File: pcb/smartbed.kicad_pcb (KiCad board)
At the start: 2 copper layers, 1 part, among them U1 ATSAMD21J18A

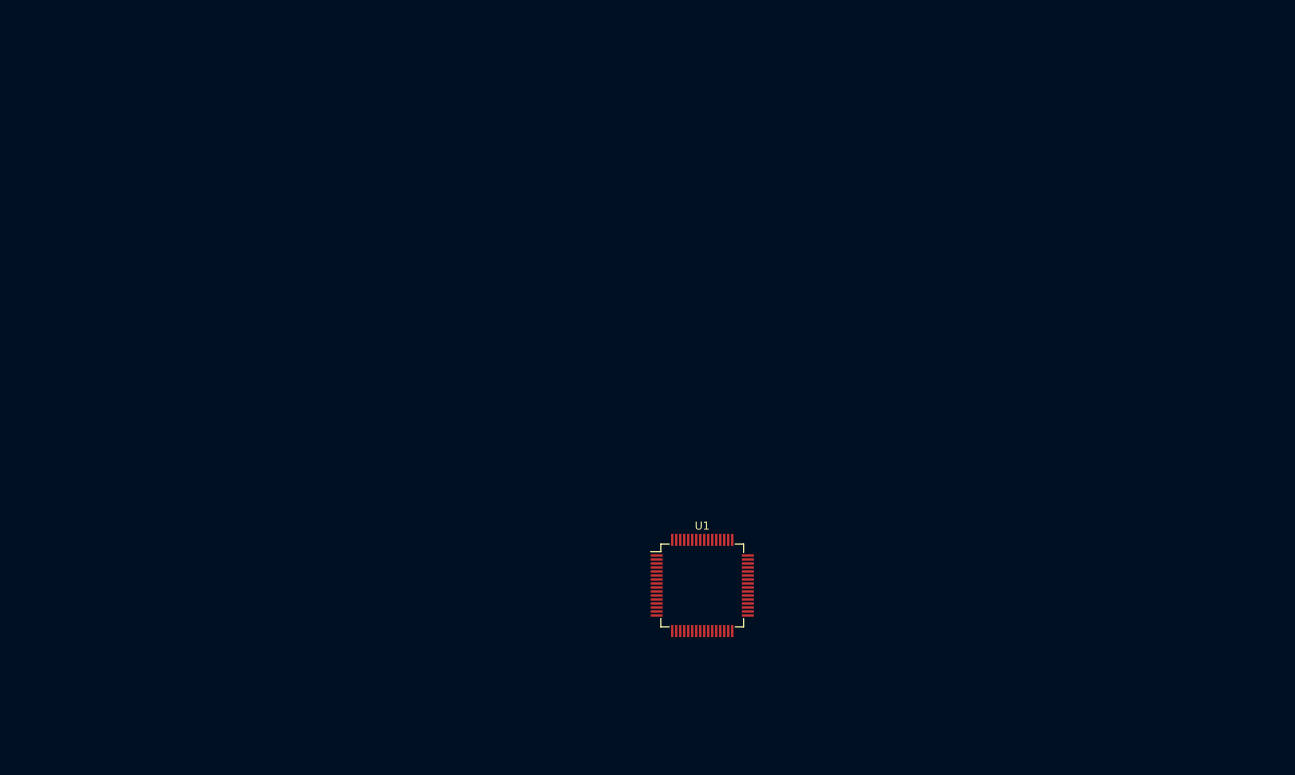
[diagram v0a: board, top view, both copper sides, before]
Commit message: Assigned footprints, started PCB
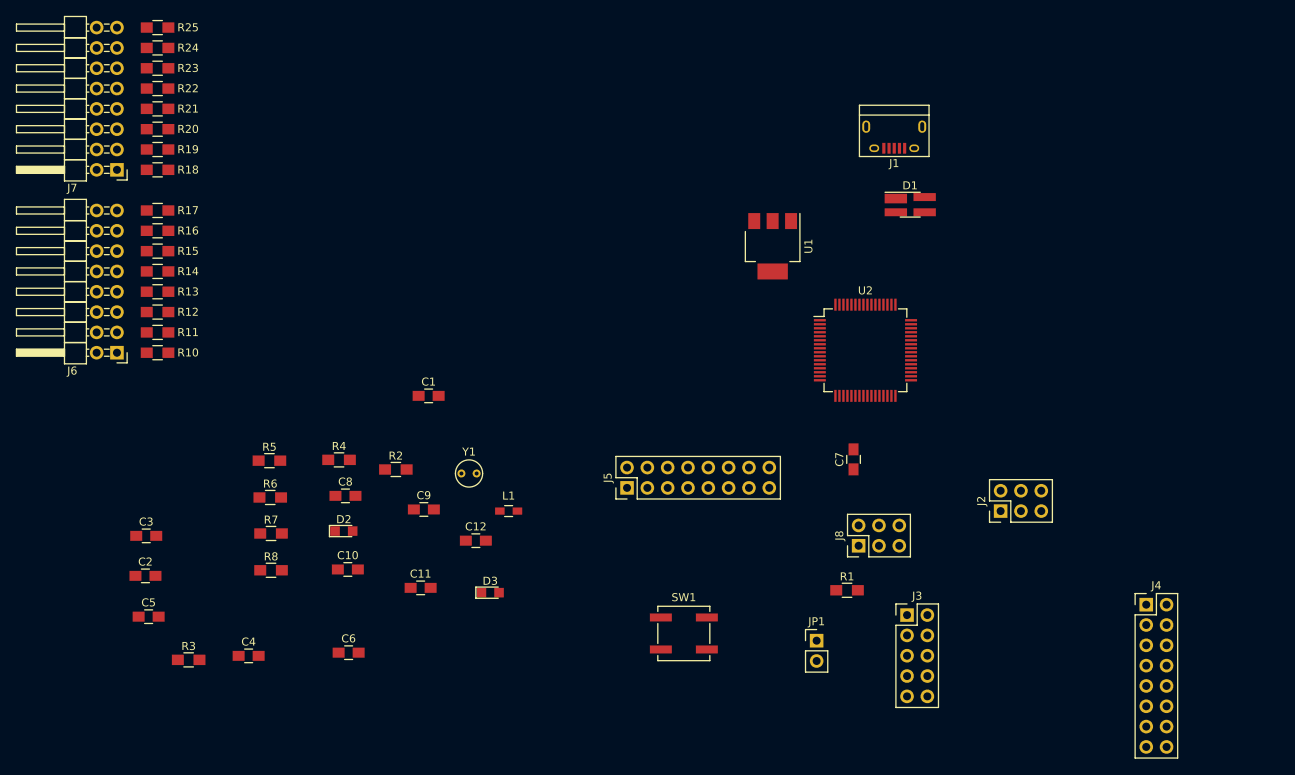
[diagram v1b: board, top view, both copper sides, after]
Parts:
- added C1: 100nF, Capacitors_SMD:C_0805_HandSoldering, F.Cu at (105.0, 83.5)
- added C10: 100nF, Capacitors_SMD:C_0805_HandSoldering, F.Cu at (94.9, 105.2)
- added C11: 100nF, Capacitors_SMD:C_0805_HandSoldering, F.Cu at (104.0, 107.5)
- added C12: 100nF, Capacitors_SMD:C_0805_HandSoldering, F.Cu at (110.9, 101.6)
- added C2: 6.8pF, Capacitors_SMD:C_0805_HandSoldering, F.Cu at (69.6, 106.0)
- added C3: 100nF, Capacitors_SMD:C_0805_HandSoldering, F.Cu at (69.7, 101.0)
- added C4: 100nF, Capacitors_SMD:C_0805_HandSoldering, F.Cu at (82.5, 116.0)
- added C5: 100nF, Capacitors_SMD:C_0805_HandSoldering, F.Cu at (70.0, 111.1)
- added C6: 6.8pF, Capacitors_SMD:C_0805_HandSoldering, F.Cu at (95.0, 115.6)
- added C7: 100nF, Capacitors_SMD:C_0805_HandSoldering, F.Cu at (158.1, 91.4)
- added C8: 10uF, Capacitors_SMD:C_0805_HandSoldering, F.Cu at (94.6, 96.0)
- added C9: 100nF, Capacitors_SMD:C_0805_HandSoldering, F.Cu at (104.4, 97.7)
- added D1: PRTR5V0U2X, TO_SOT_Packages_SMD:SOT-143_Handsoldering, F.Cu at (165.2, 59.6)
- added D2: LED G, LEDs:LED_0805, F.Cu at (94.4, 100.4)
- added D3: LED G, LEDs:LED_0805, F.Cu at (112.7, 108.1)
- added J1: USB_MICRO_A, Connectors:USB_Micro-B, F.Cu at (163.2, 51.2)
- added J2: SBBUS_1, Pin_Headers:Pin_Header_Straight_2x03_Pitch2.54mm, F.Cu at (176.5, 97.9)
- added J3: DBGCON, Pin_Headers:Pin_Header_Straight_2x05_Pitch2.54mm, F.Cu at (164.8, 110.9)
- added J4: GPIOCON, Pin_Headers:Pin_Header_Straight_2x08_Pitch2.54mm, F.Cu at (194.7, 109.6)
- added J5: GPIOCON, Pin_Headers:Pin_Header_Straight_2x08_Pitch2.54mm, F.Cu at (129.8, 95.0)
- added J6: FSRCON1, Pin_Headers:Pin_Header_Angled_2x08_Pitch2.54mm, F.Cu at (66.0, 78.1)
- added J7: FSRCON2, Pin_Headers:Pin_Header_Angled_2x08_Pitch2.54mm, F.Cu at (66.0, 55.2)
- added J8: SBBUS_2, Pin_Headers:Pin_Header_Straight_2x03_Pitch2.54mm, F.Cu at (158.8, 102.2)
- added JP1: JMP, Pin_Headers:Pin_Header_Straight_1x02_Pitch2.54mm, F.Cu at (153.5, 114.1)
- added L1: FeBead, Inductors_SMD:L_0603_HandSoldering, F.Cu at (115.0, 97.9)
- added R1: 4.7K, Resistors_SMD:R_0805_HandSoldering, F.Cu at (157.3, 107.8)
- added R10: 10K, Resistors_SMD:R_0805_HandSoldering, F.Cu at (71.1, 78.1)
- added R11: 10K, Resistors_SMD:R_0805_HandSoldering, F.Cu at (71.1, 75.6)
- added R12: 10K, Resistors_SMD:R_0805_HandSoldering, F.Cu at (71.1, 73.0)
- added R13: 10K, Resistors_SMD:R_0805_HandSoldering, F.Cu at (71.1, 70.5)
- added R14: 10K, Resistors_SMD:R_0805_HandSoldering, F.Cu at (71.1, 67.9)
- added R15: 10K, Resistors_SMD:R_0805_HandSoldering, F.Cu at (71.1, 65.4)
- added R16: 10K, Resistors_SMD:R_0805_HandSoldering, F.Cu at (71.1, 62.9)
- added R17: 10K, Resistors_SMD:R_0805_HandSoldering, F.Cu at (71.1, 60.3)
- added R18: 10K, Resistors_SMD:R_0805_HandSoldering, F.Cu at (71.1, 55.2)
- added R19: 10K, Resistors_SMD:R_0805_HandSoldering, F.Cu at (71.1, 52.7)
- added R2: 100k, Resistors_SMD:R_0805_HandSoldering, F.Cu at (100.9, 92.7)
- added R20: 10K, Resistors_SMD:R_0805_HandSoldering, F.Cu at (71.1, 50.2)
- added R21: 10K, Resistors_SMD:R_0805_HandSoldering, F.Cu at (71.1, 47.6)
- added R22: 10K, Resistors_SMD:R_0805_HandSoldering, F.Cu at (71.1, 45.1)
- added R23: 10K, Resistors_SMD:R_0805_HandSoldering, F.Cu at (71.1, 42.5)
- added R24: 10K, Resistors_SMD:R_0805_HandSoldering, F.Cu at (71.1, 40.0)
- added R25: 10K, Resistors_SMD:R_0805_HandSoldering, F.Cu at (71.1, 37.5)
- added R3: 4.7K, Resistors_SMD:R_0805_HandSoldering, F.Cu at (75.0, 116.5)
- added R4: 39R, Resistors_SMD:R_0805_HandSoldering, F.Cu at (93.8, 91.5)
- added R5: 30k, Resistors_SMD:R_0805_HandSoldering, F.Cu at (85.1, 91.6)
- added R6: 47k, Resistors_SMD:R_0805_HandSoldering, F.Cu at (85.2, 96.2)
- added R7: 330R, Resistors_SMD:R_0805_HandSoldering, F.Cu at (85.3, 100.7)
- added R8: 330R, Resistors_SMD:R_0805_HandSoldering, F.Cu at (85.3, 105.3)
- added SW1: SW_SPST, Buttons_Switches_SMD:SW_SPST_B3SL-1002P, F.Cu at (136.9, 113.2)
- added U2: ATSAMD21J18A, Housings_QFP:TQFP-64_10x10mm_Pitch0.5mm, F.Cu at (159.6, 77.8)
- added Y1: 32.768kHz, Crystals:Crystal_Round_d3.0mm_Vertical, F.Cu at (109.1, 93.2)
- U1: value ATSAMD21J18A -> LD1117S33CTR; footprint Housings_QFP:TQFP-64_10x10mm_Pitch0.5mm -> TO_SOT_Packages_SMD:SOT-223
- moved U1 43.3 mm to (148.0, 64.8), turned to 270 degrees
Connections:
- U1 pad 1: Net-(U1-Pad1) -> GND
- U1 pad 2: Net-(U1-Pad2) -> +3V3
- U1 pad 3: Net-(U1-Pad3) -> +5V
- U1 pad 4: Net-(U1-Pad4) -> (no net)

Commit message: Biggest part of board done
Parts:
- C1, C10, C11, C12, C2, C3, C4, C5, C6, C7, C8, C9: footprint Capacitors_SMD:C_0805_HandSoldering -> Capacitors_SMD:C_0603_HandSoldering
- moved J7 133.5 mm to (198.7, 69.9), turned to 0 degrees
- moved R24 132.4 mm to (195.9, 84.4), turned to 90 degrees
- moved R25 131.6 mm to (193.6, 85.7), turned to 90 degrees
- moved R22 129.3 mm to (195.9, 79.0), turned to 90 degrees
- moved R23 128.2 mm to (193.6, 80.3), turned to 90 degrees
- moved R20 127.0 mm to (195.9, 73.7), turned to 90 degrees
- moved R21 125.5 mm to (193.6, 75.0), turned to 90 degrees
- moved R18 125.5 mm to (195.9, 68.4), turned to 270 degrees
- moved R19 123.7 mm to (193.6, 69.7), turned to 90 degrees
- moved R8 119.3 mm to (191.8, 51.5), turned to 270 degrees
- moved C4 116.1 mm to (181.5, 55.3), turned to 270 degrees
- moved R7 115.0 mm to (189.2, 51.5), turned to 270 degrees
- moved D2 104.5 mm to (189.2, 56.5), turned to 90 degrees
- moved C3 98.3 mm to (157.5, 56.8), turned to 90 degrees
- moved D3 94.4 mm to (191.8, 56.5), turned to 90 degrees
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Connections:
- D1 pad 2: D+ -> D-
- D1 pad 3: D- -> D+
- J6 pad 1: FSR0 -> FSR7
- J6 pad 11: FSR5 -> FSR2
- J6 pad 13: FSR6 -> FSR1
- J6 pad 15: FSR7 -> FSR0
- J6 pad 3: FSR1 -> FSR6
- J6 pad 5: FSR2 -> FSR5
- J6 pad 7: FSR3 -> FSR4
- J6 pad 9: FSR4 -> FSR3
- R10 pad 1: FSR0 -> FSR7
- R11 pad 1: FSR1 -> FSR6
- R12 pad 1: FSR2 -> FSR5
- R13 pad 1: FSR3 -> FSR4
- R14 pad 1: FSR4 -> FSR3
- R15 pad 1: FSR5 -> FSR2
- R16 pad 1: FSR6 -> FSR1
- R17 pad 1: FSR7 -> FSR0
- U2 pad 10: FSR15 -> FSR1
- U2 pad 3: FSR0 -> FSR12
- U2 pad 4: FSR1 -> FSR13
- U2 pad 5: FSR12 -> FSR14
- U2 pad 6: FSR13 -> FSR15
- U2 pad 9: FSR14 -> FSR0
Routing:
- net GND: track 0.00 -> 374.7 mm, vias 0 -> 4
- net +3V3: track 0.00 -> 233.2 mm, vias 0 -> 7
- net +5V: track 0.00 -> 95.1 mm, vias 0 -> 1
- net FSR15: track 0.00 -> 49.8 mm, vias 0 -> 2
- net FSR14: track 0.00 -> 49.4 mm, vias 0 -> 2
- net FSR13: track 0.00 -> 48.2 mm, vias 0 -> 2
- net RESET: track 0.00 -> 47.8 mm, vias 0 -> 2
- net FSR8: track 0.00 -> 47.7 mm, vias 0 -> 2
- net FSR12: track 0.00 -> 47.5 mm, vias 0 -> 2
- net FSR11: track 0.00 -> 46.9 mm, vias 0 -> 2
- net FSR9: track 0.00 -> 45.9 mm, vias 0 -> 2
- net FSR10: track 0.00 -> 45.0 mm, vias 0 -> 2
- net DBGLED: track 0.00 -> 44.6 mm, vias 0 -> 2
- net FSR6: track 0.00 -> 43.3 mm
- net FSR7: track 0.00 -> 43.3 mm
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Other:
- net class PWR added: clearance 0.2, trace_width 0.4, via_dia 0.6, via_drill 0.4
- net class uProc added: clearance 0.1, trace_width 0.1, via_dia 0.6, via_drill 0.4
- rule trace_min: 0.2 -> 0.1

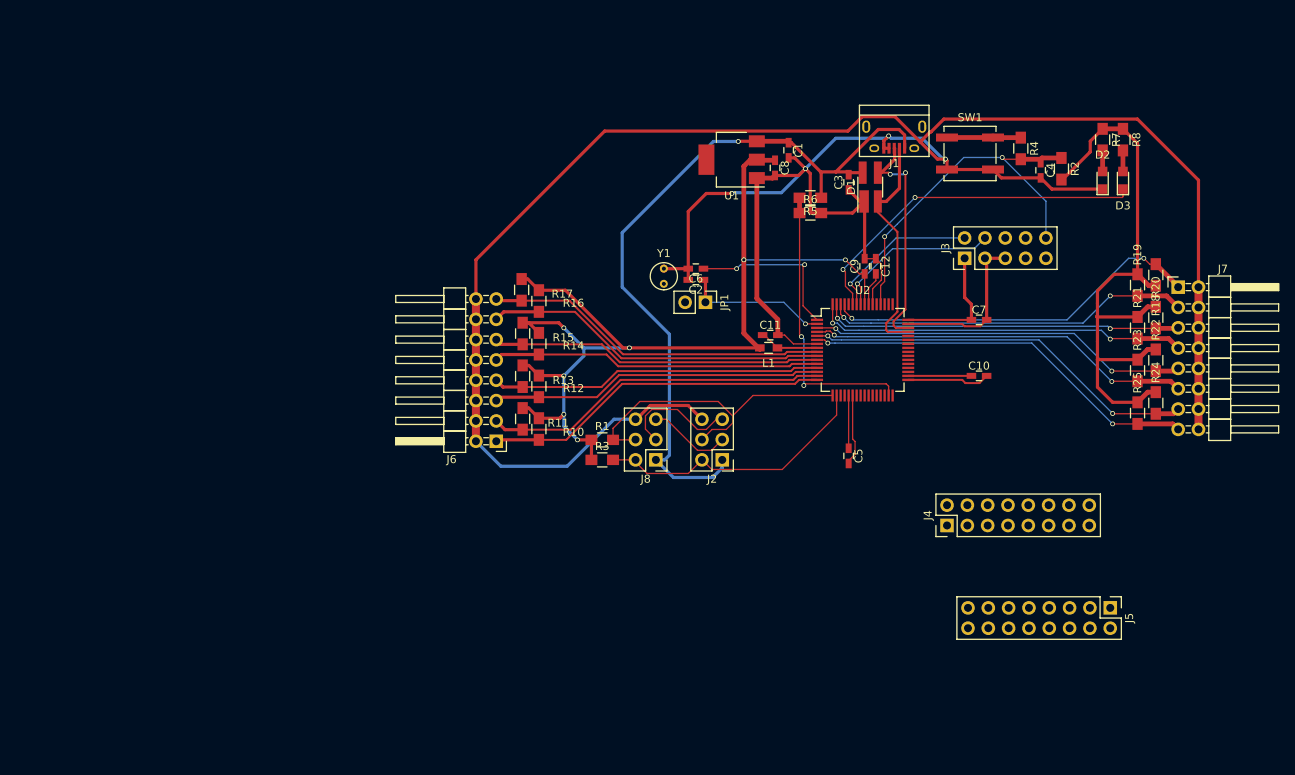
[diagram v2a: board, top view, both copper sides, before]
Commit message: Connected most of the traces
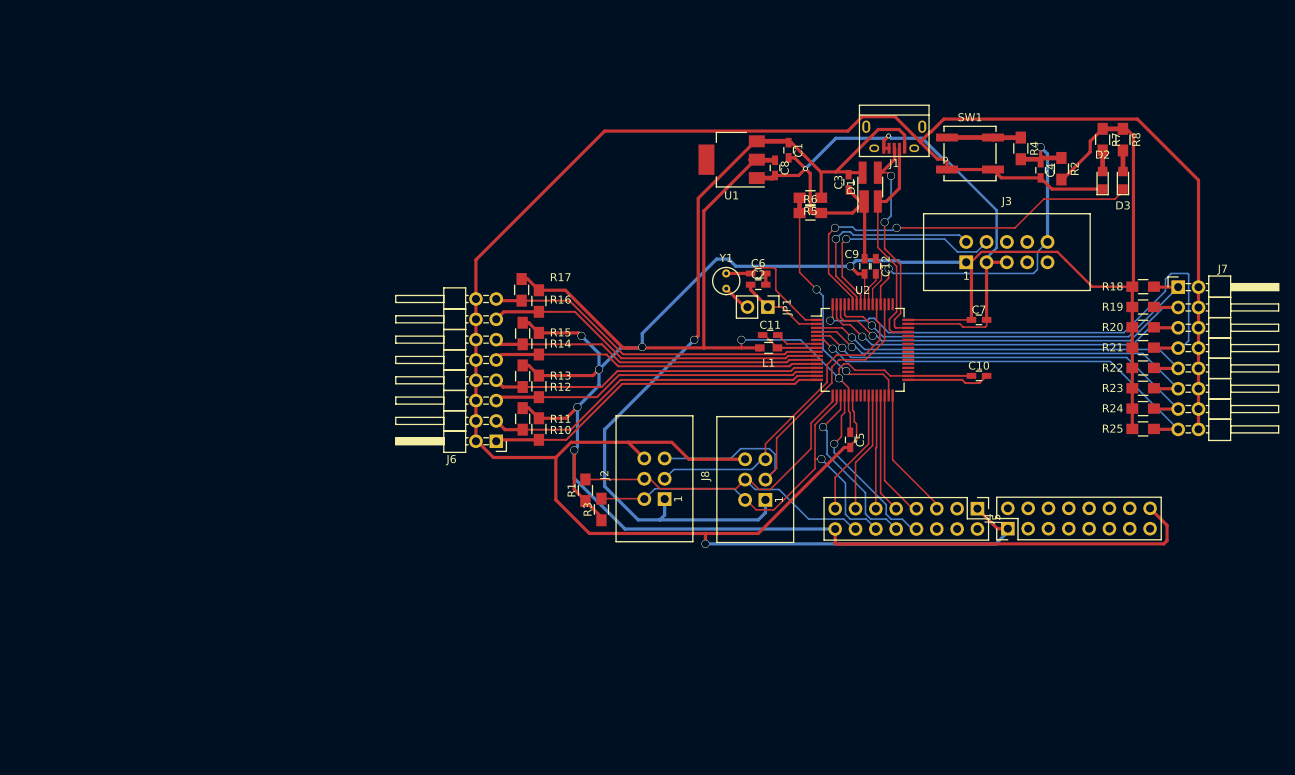
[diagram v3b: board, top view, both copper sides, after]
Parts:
- J2, J8: footprint Pin_Headers:Pin_Header_Straight_2x03_Pitch2.54mm -> Connectors:IDC_Header_Straight_6pins
- J3: footprint Pin_Headers:Pin_Header_Straight_2x05_Pitch2.54mm -> Connectors:IDC_Header_Straight_10pins
- Y1: value 32.768kHz -> Crystal
- moved J5 20.7 mm to (173.6, 97.6)
- moved J8 14.6 mm to (147.1, 96.5), turned to 90 degrees
- moved J2 8.71 mm to (134.5, 96.4), turned to 90 degrees
- moved JP1 7.82 mm to (147.4, 72.4)
- moved C6 7.82 mm to (146.2, 68.2), turned to 0 degrees
- moved C2 7.82 mm to (146.2, 69.6), turned to 0 degrees
- moved Y1 7.82 mm to (142.2, 70.1)
- moved J4 7.61 mm to (177.4, 100.1)
- moved R1 6.64 mm to (124.6, 95.3), turned to 90 degrees
- moved R3 6.20 mm to (126.6, 97.7), turned to 90 degrees
- moved R19 2.83 mm to (194.3, 72.4), turned to 180 degrees
- moved R21 2.58 mm to (194.3, 77.5), turned to 180 degrees
- moved R23 2.34 mm to (194.3, 82.5), turned to 180 degrees
- moved R18 2.16 mm to (194.3, 69.8), turned to 180 degrees
- moved R25 2.10 mm to (194.3, 87.6), turned to 180 degrees
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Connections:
- C2 pad 2: GND -> Net-(C2-Pad2)
- C6 pad 2: GND -> Net-(C2-Pad2)
- Y1 pad 2: GND -> XIN
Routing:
- net +3V3: track 233.2 -> 391.9 mm, vias 7 -> 8
- net GND: track 374.7 -> 438.7 mm
- net SENSE_OUT: track 15.0 -> 48.3 mm
- net SENSE_IN: track 10.5 -> 41.1 mm
- net PA11: track 0.00 -> 22.6 mm, vias 0 -> 1
- net PA10: track 0.00 -> 22.5 mm, vias 0 -> 1
- net SCL: track 35.3 -> 54.3 mm, vias 0 -> 1
- net FSR11: track 46.9 -> 64.9 mm, vias 2 -> 1
- net PA15: track 0.00 -> 16.4 mm
- net PA13: track 0.00 -> 16.1 mm
- net SDA: track 40.5 -> 56.6 mm
- net PB13: track 0.00 -> 15.9 mm
- net PB14: track 0.00 -> 15.0 mm
- net PA12: track 0.00 -> 15.0 mm
- net PB15: track 0.00 -> 14.2 mm
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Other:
- net class Default: trace_width 0.25 -> 0.2; via_dia 0.6 -> 1; via_drill 0.4 -> 0.9
- net class PWR removed
- net class uProc removed
- rule trace_min: 0.1 -> 0.2
- rule via_min_drill: 0.3 -> 0.9
- rule via_min_size: 0.4 -> 0.6

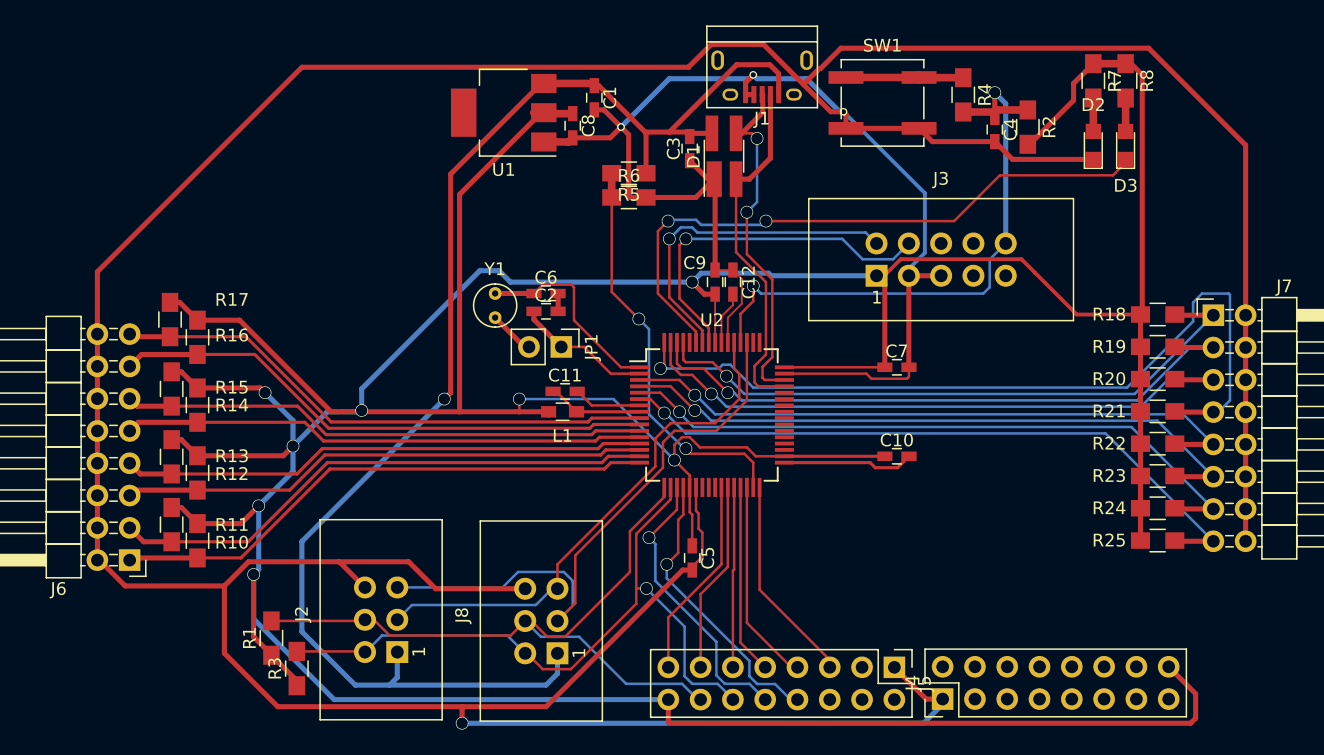
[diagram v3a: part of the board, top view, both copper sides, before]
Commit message: Routed the board
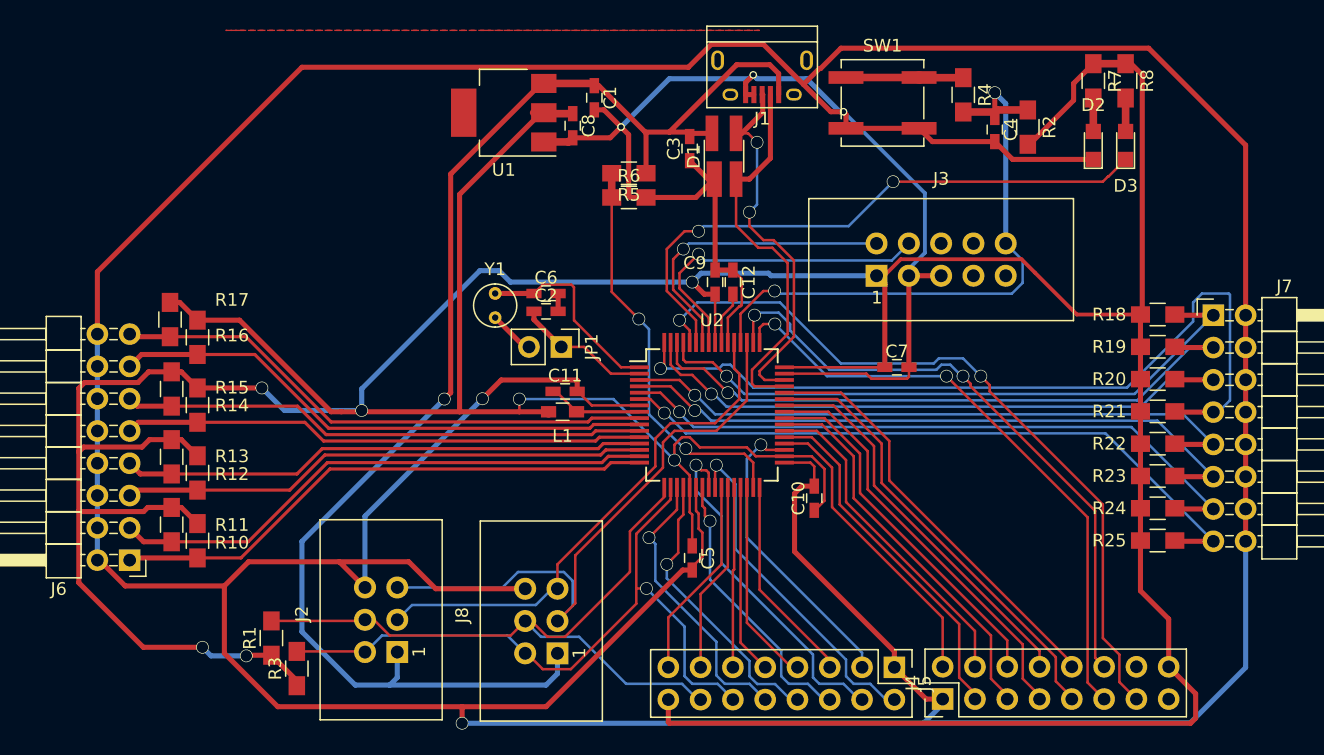
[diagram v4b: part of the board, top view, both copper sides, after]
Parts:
- moved C10 7.29 mm to (167.3, 84.3), turned to 90 degrees
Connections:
- J4 pad 10: PA17 -> PA23
- J4 pad 11: PA22 -> PB22
- J4 pad 12: SENSE_IN -> PB23
- J4 pad 13: PA20 -> PB31
- J4 pad 14: SENSE_OUT -> Net-(J4-Pad14)
- J4 pad 15: PA21 -> Net-(J4-Pad15)
- J4 pad 2: PB17 -> PA17
- J4 pad 3: PB31 -> PA18
- J4 pad 4: PB16 -> PA19
- J4 pad 5: PB23 -> PB16
- J4 pad 6: PA19 -> PB17
- J4 pad 7: PB22 -> PA20
- J4 pad 8: PA18 -> PA21
- J4 pad 9: PA23 -> PA22
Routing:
- net GND: track 438.7 -> 515.8 mm, vias 4 -> 5
- net PB31: track 0.00 -> 59.6 mm, vias 0 -> 2
- net PB23: track 0.00 -> 48.8 mm, vias 0 -> 2
- net PB22: track 0.00 -> 48.2 mm, vias 0 -> 2
- net PA22: track 0.00 -> 35.4 mm
- net PA23: track 0.00 -> 33.5 mm
- net PA20: track 0.00 -> 32.9 mm
- net PA21: track 0.00 -> 31.1 mm
- net PB16: track 0.00 -> 30.6 mm
- net PB17: track 0.00 -> 28.7 mm
- net PA18: track 0.00 -> 28.1 mm
- net PB11: track 0.00 -> 27.6 mm, vias 0 -> 1
- net PB12: track 0.00 -> 27.2 mm, vias 0 -> 1
- net PA19: track 0.00 -> 26.3 mm
- net PA17: track 0.00 -> 23.8 mm
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- added copper zone on F.Cu, net GND
